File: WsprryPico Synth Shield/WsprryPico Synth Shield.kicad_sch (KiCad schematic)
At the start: 54 parts, among them J11 1x20 socket, J12 1x20 socket, J61 SMA 50ohm, J71 QLG3 GPS Receiver, Q61 BS170, SW81 Push, U31 Si5351A-B-GTR, U41 TPS7A2033, U51 TPS22918, U71 LS7366R-S, U72 SN74LVC1G14, Y21 25MHz TCXO

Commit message: Save Synth layout progress and localize TP71 through-hole footprint
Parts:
- TP71: footprint wsprrypico-synth-shield:TestPoint_Pad_D2.0mm -> wsprrypico-synth-shield:TestPoint_THTPad_1.0x1.0mm_Drill0.5mm
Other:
- moved on the sheet: R73
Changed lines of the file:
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@@
 	)
 	(junction
+		(at 142.24 177.8)
+		(diameter 0)
+		(color 0 0 0 0)
+	)
+	(junction
 		(at 125.73 27.94)
 		(diameter 0)
@@
 		(color 0 0 0 0)
 	)
+	(junction
+		(at 123.19 182.88)
+		(diameter 0)
+		(color 0 0 0 0)
+	)
 	(no_connect
 		(at 189.23 41.91)
@@
 	(wire
 		(pts
+			(xy 124.46 182.88) (xy 123.19 182.88)
+		)
+		(stroke
+			(width 0)
+			(type default)
+		)
+	)
+	(wire
+		(pts
 			(xy 354.33 93.98) (xy 365.76 93.98)
 		)
@@
 	(wire
 		(pts
+			(xy 123.19 182.88) (xy 123.19 177.8)
+		)
+		(stroke
+			(width 0)
+			(type default)
+		)
+	)
+	(wire
+		(pts
 			(xy 158.75 52.07) (xy 170.18 52.07)
 		)
@@
 	(wire
 		(pts
+			(xy 116.84 177.8) (xy 123.19 177.8)
+		)
+		(stroke
+			(width 0)
+			(type default)
+		)
+	)
+	(wire
+		(pts
 			(xy 86.36 138.43) (xy 78.74 138.43)
 		)
@@
 	(wire
 		(pts
+			(xy 143.51 180.34) (xy 142.24 180.34)
+		)
+		(stroke
+			(width 0)
+			(type default)
+		)
+	)
+	(wire
+		(pts
 			(xy 228.6 104.14) (xy 229.87 104.14)
 		)
@@
 	(wire
 		(pts
+			(xy 142.24 177.8) (xy 135.89 177.8)
+		)
+		(stroke
+			(width 0)
+			(type default)
+		)
+	)
+	(wire
+		(pts
 			(xy 138.43 105.41) (xy 138.43 106.68)
 		)
@@
 	(wire
 		(pts
-			(xy 109.22 182.88) (xy 109.22 184.15)
+			(xy 113.03 182.88) (xy 113.03 184.15)
 		)
 		(stroke
@@
 	(wire
 		(pts
+			(xy 138.43 185.42) (xy 143.51 185.42)
+		)
+		(stroke
+			(width 0)
+			(type default)
+		)
+	)
+	(wire
+		(pts
 			(xy 111.76 104.14) (xy 111.76 96.52)
 		)
@@
 	(wire
 		(pts
+			(xy 123.19 182.88) (xy 121.92 182.88)
+		)
+		(stroke
+			(width 0)
+			(type default)
+		)
+	)
+	(wire
+		(pts
 			(xy 90.17 31.75) (xy 90.17 33.02)
 		)
@@
 	(wire
 		(pts
+			(xy 142.24 180.34) (xy 142.24 177.8)
+		)
+		(stroke
+			(width 0)
+			(type default)
+		)
+	)
+	(wire
+		(pts
 			(xy 279.4 41.91) (xy 284.48 41.91)
 		)
@@
 	(wire
 		(pts
-			(xy 110.49 182.88) (xy 109.22 182.88)
+			(xy 114.3 182.88) (xy 113.03 182.88)
 		)
 		(stroke
@@
 	(wire
 		(pts
-			(xy 118.11 182.88) (xy 124.46 182.88)
-		)
-		(stroke
-			(width 0)
-			(type default)
-		)
-	)
-	(wire
-		(pts
 			(xy 111.76 96.52) (xy 110.49 96.52)
 		)
@@
 	(wire
 		(pts
-			(xy 143.51 177.8) (xy 135.89 177.8)
+			(xy 143.51 177.8) (xy 142.24 177.8)
 		)
 		(stroke
@@
 	)
 	(label "GPS_PPS"
-		(at 118.11 182.88 0)
+		(at 116.84 177.8 0)
 		(effects
 			(font
@@
 	)
 	(label "GPS_TX"
-		(at 143.51 185.42 180)
+		(at 138.43 185.42 0)
 		(effects
 			(font
 				(size 1 1)
 			)
-			(justify right bottom)
+			(justify left bottom)
 		)
 	)
@@
 	)
 	(label "GND"
-		(at 110.49 182.88 180)
+		(at 114.3 182.88 180)
 		(effects
 			(font
@@
 		)
 	)
-	(label "PICO_3V3"
-		(at 143.51 180.34 180)
-		(effects
-			(font
-				(size 1 1)
-			)
-			(justify right bottom)
-		)
-	)
 	(label "GND"
 		(at 123.19 55.88 180)
@@
 	(symbol
 		(lib_id "wsprrypico-synth-shield:R")
-		(at 114.3 182.88 180)
+		(at 118.11 182.88 180)
 		(unit 1)
 		(body_style 1)
@@
 		(dnp no)
 		(property "Reference" "R73"
-			(at 116.078 185.166 0)
+			(at 119.888 185.166 0)
 			(show_name no)
 			(do_not_autoplace no)
@@
 		)
 		(property "Value" "100kΩ"
-			(at 117.094 180.34 0)
+			(at 120.904 180.34 0)
 			(show_name no)
 			(do_not_autoplace no)
@@
 		)
 		(property "Footprint" "wsprrypico-synth-shield:R_0603_1608Metric"
-			(at 114.3 182.88 0)
+			(at 118.11 182.88 0)
 			(hide yes)
 			(show_name no)
@@
 		)
 		(property "Datasheet" "https://www.lcsc.com/product-detail/C25803.html"
-			(at 114.3 182.88 0)
+			(at 118.11 182.88 0)
 			(hide yes)
 			(show_name no)
@@
 		)
 		(property "Description" "PPS input default pull-down; 100 kohm; Thick film"
-			(at 114.3 182.88 0)
+			(at 118.11 182.88 0)
 			(hide yes)
 			(show_name no)
@@
 		)
 		(property "Manufacturer" "UNI-ROYAL"
-			(at 114.3 182.88 0)
+			(at 118.11 182.88 0)
 			(hide yes)
 			(show_name no)
@@
 		)
 		(property "MPN" "0603WAF1003T5E"
-			(at 114.3 182.88 0)
+			(at 118.11 182.88 0)
 			(hide yes)
 			(show_name no)
@@
 		)
 		(property "LCSC Part #" "C25803"
-			(at 114.3 182.88 0)
+			(at 118.11 182.88 0)
 			(hide yes)
 			(show_name no)
@@
 		)
 		(property "Supplier URL" "https://www.lcsc.com/product-detail/C25803.html"
-			(at 114.3 182.88 0)
+			(at 118.11 182.88 0)
 			(hide yes)
 			(show_name no)
@@
 		)
 		(property "Specified Value" "100 kohm"
-			(at 114.3 182.88 0)
+			(at 118.11 182.88 0)
 			(hide yes)
 			(show_name no)
@@
 		)
 		(property "Technology" "Thick film"
-			(at 114.3 182.88 0)
+			(at 118.11 182.88 0)
 			(hide yes)
 			(show_name no)
@@
 		)
 		(property "Tolerance" "1%"
-			(at 114.3 182.88 0)
+			(at 118.11 182.88 0)
 			(hide yes)
 			(show_name no)
@@
 		)
 		(property "Rating" "100 mW; 75 V"
-			(at 114.3 182.88 0)
+			(at 118.11 182.88 0)
 			(hide yes)
 			(show_name no)
@@
 		)
 		(property "Assembly" "SMT"
-			(at 114.3 182.88 0)
+			(at 118.11 182.88 0)
 			(hide yes)
 			(show_name no)
@@
 		)
 		(property "Function" "PPS input default pull-down"
-			(at 114.3 182.88 0)
+			(at 118.11 182.88 0)
 			(hide yes)
 			(show_name no)
@@
 		)
 		(property "Selection status" "Selected prototype"
-			(at 114.3 182.88 0)
+			(at 118.11 182.88 0)
 			(hide yes)
 			(show_name no)
@@
 			)
 		)
-		(property "Footprint" "wsprrypico-synth-shield:TestPoint_Pad_D2.0mm"
+		(property "Footprint" "wsprrypico-synth-shield:TestPoint_THTPad_1.0x1.0mm_Drill0.5mm"
 			(at 135.89 146.05 0)
 			(hide yes)
@@
 	(symbol
 		(lib_id "power:GND")
-		(at 109.22 184.15 0)
+		(at 113.03 184.15 0)
 		(mirror y)
 		(unit 1)
@@
 		(dnp no)
 		(property "Reference" "#PWR029"
-			(at 109.22 190.5 0)
+			(at 113.03 190.5 0)
 			(hide yes)
 			(show_name no)
@@
 		)
 		(property "Value" "GND"
-			(at 109.22 187.96 0)
+			(at 113.03 187.96 0)
 			(show_name no)
 			(do_not_autoplace no)
@@
 		)
 		(property "Footprint" ""
-			(at 109.22 184.15 0)
+			(at 113.03 184.15 0)
 			(hide yes)
 			(show_name no)
@@
 		)
 		(property "Datasheet" ""
-			(at 109.22 184.15 0)
+			(at 113.03 184.15 0)
 			(hide yes)
 			(show_name no)
@@
 		)
 		(property "Description" "Power symbol creates a global label with name \"GND\" , ground"
-			(at 109.22 184.15 0)
+			(at 113.03 184.15 0)
 			(hide yes)
 			(show_name no)

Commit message: Add onboard 90-series GPS receiver to Pico synth shield
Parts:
- removed J71: QLG3 GPS Receiver, wsprrypico-synth-shield:QLG3_GPS_UndersideHeader_SinglePost, symbol wsprrypico-synth-shield:Conn_01x05
- added C92, C93: 100nF, wsprrypico-synth-shield:C_0603_1608Metric, symbol wsprrypico-synth-shield:C
- added J91: SMA 50ohm, wsprrypico-synth-shield:SMA_Adafruit_1865_EdgeMount, symbol wsprrypico-synth-shield:SMA
- added L91: 47nH, wsprrypico-synth-shield:L_0603_1608Metric, symbol wsprrypico-synth-shield:L
- added R91: 1kΩ, wsprrypico-synth-shield:R_0603_1608Metric, symbol wsprrypico-synth-shield:R
- added U91: ATGM336H-5N31, wsprrypico-synth-shield:Zhongke_ATGM336H-5N31_9.7x10.1mm_P1.1mm, symbol wsprrypico-synth-shield:ATGM336H_5N31
- C91: renamed from C74; value 2.2μF -> 10uF; footprint wsprrypico-synth-shield:C_0805_2012Metric -> wsprrypico-synth-shield:C_1206_3216Metric; Function GPS header local supply bypass -> GNSS supply bulk; LCSC Part # C364318 -> C77093; MPN CL21B225KAFNFNE -> GRM31CR71E106KA12L; Manufacturer Samsung Electro-Mechanics -> muRata; Specified Value 2.2 uF -> 10 uF; Supplier URL https://www.lcsc.com/product-detail/C364318.html -> https://www.lcsc.com/product-detail/C77093.html
- JP41: footprint wsprrypico-synth-shield:PowerSelector_VBUS_IN_VSYS_Cuttable -> Jumper:SolderJumper-3_P1.3mm_Bridged12_RoundedPad1.0x1.5mm_NumberLabels
- renumbered TP71 to TP91
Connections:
- net GND: now also C92.2, C93.2, J91.2 (GND), U91.1 (GND), U91.10 (GND), U91.12 (GND)
- net GPS_PPS_RAW: now also U91.4 (1PPS)
- net GPS_RX: now also R91.2
- net GPS_TX: now also U91.2 (TXD)
- net PICO_3V3: now also C92.1, C93.1, U91.6 (VBAT), U91.8 (VCC)
- new net GPS_ANT: J91.1 (In), L91.2, U91.11 (RF_IN)
- new net GPS_ANT_BIAS: L91.1, U91.14 (VCC_RF)
- new net GPS_RX_MODULE: R91.1, U91.3 (RXD)
- no-connect marks 20 -> 28
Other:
- note added: "3.3 V UART/PPS. VBAT tied to PICO_3V3; no battery. Active antenna: 47 nH bias feed; 50-ohm RF route. CASIC commands, not GK9501."
- note added: "PPS from 90-series GPS receiver. Counter and PPS conditioner retain 70-series references."
- note removed: "QLG3 underside male pins -> shield TOP female socket. 1=3V3 2=VBAT(3V3) 3=PPS 4=GPS_TX 5=GND"
- moved on the sheet: C91, TP91

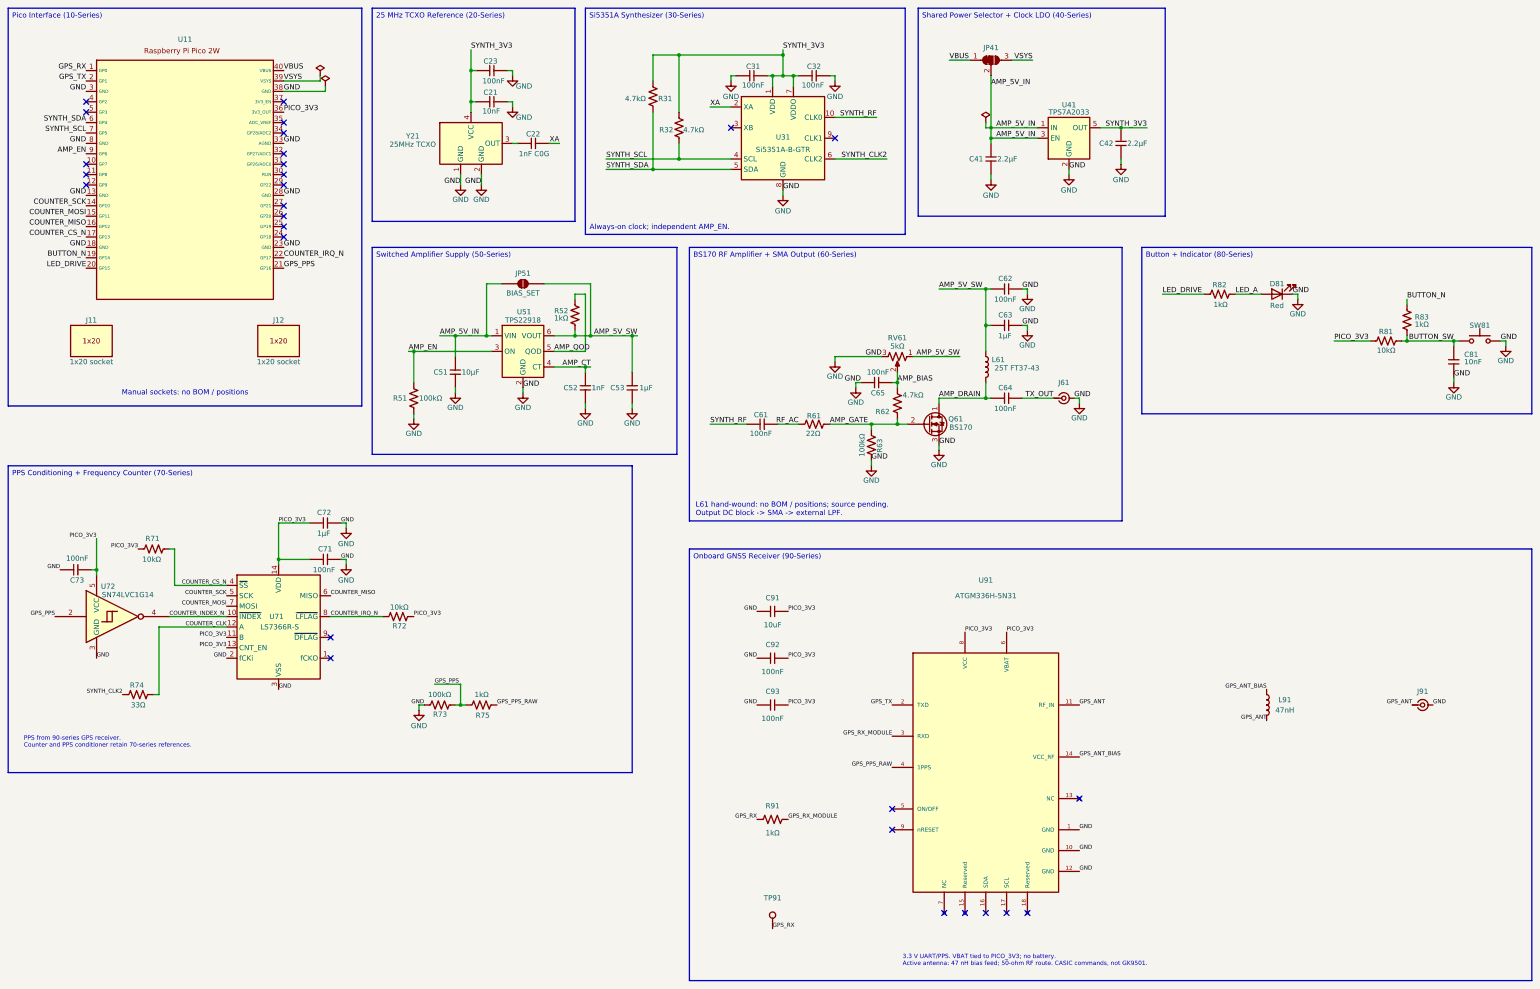
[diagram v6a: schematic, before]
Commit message: Checked through the JLCPCB upload
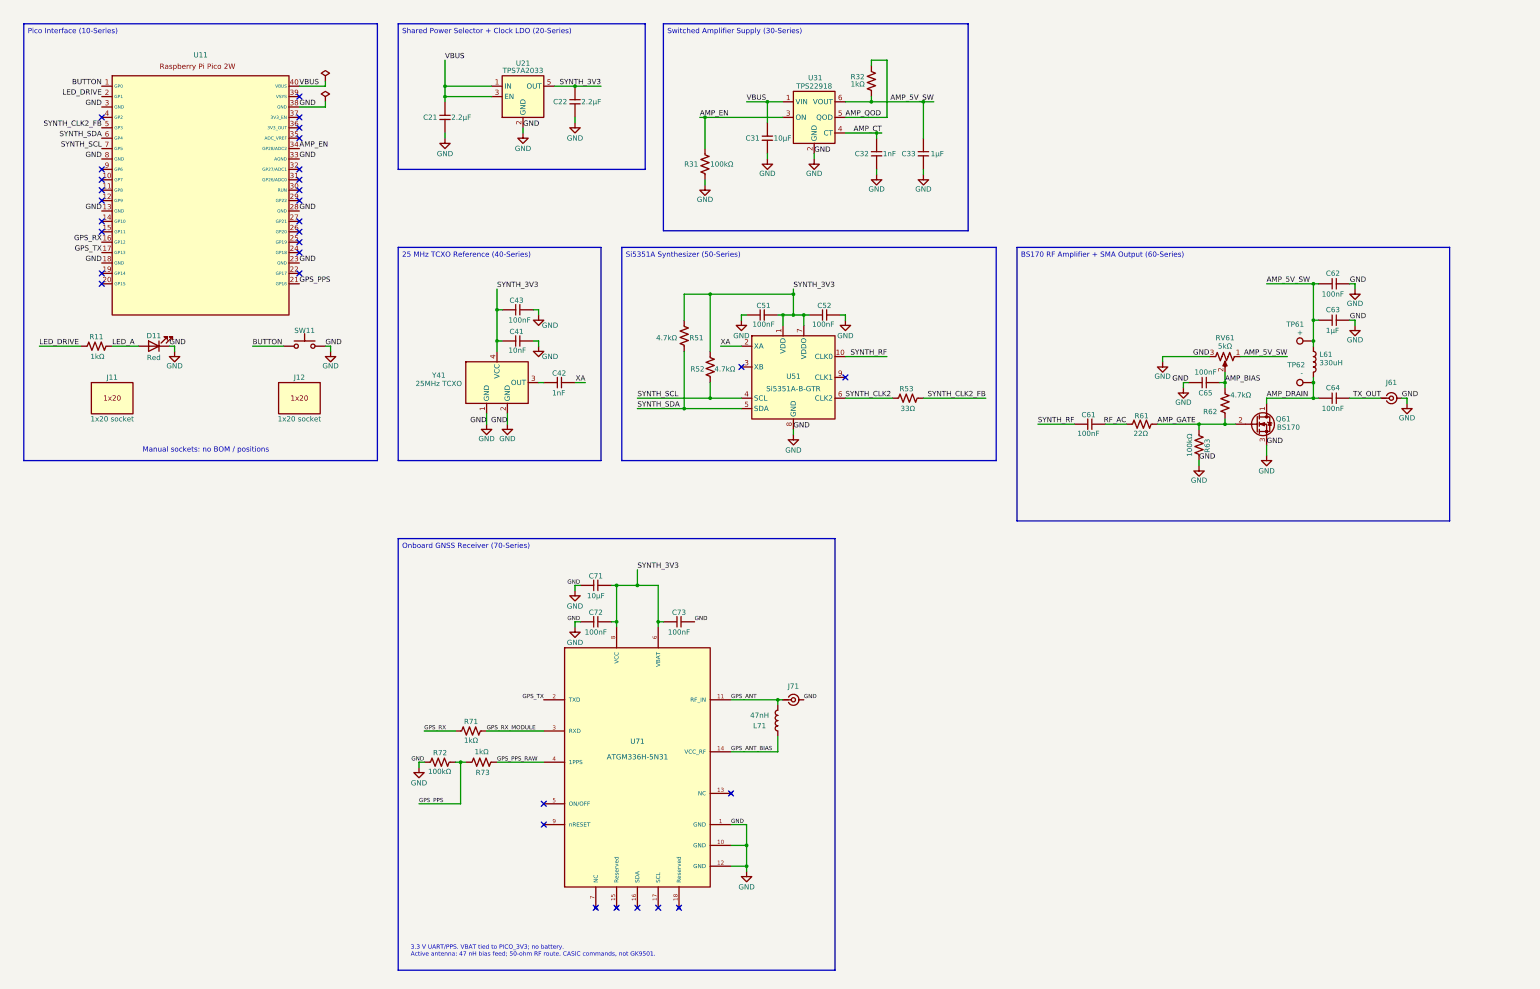
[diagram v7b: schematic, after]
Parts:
- removed C71, C73: 100nF, wsprrypico-synth-shield:C_0603_1608Metric, symbol wsprrypico-synth-shield:C
- removed C72: 1μF, wsprrypico-synth-shield:C_0805_2012Metric, symbol wsprrypico-synth-shield:C
- removed C81: 10nF, wsprrypico-synth-shield:C_0603_1608Metric, symbol wsprrypico-synth-shield:C
- removed JP41: SolderJumper_3_Bridged12, Jumper:SolderJumper-3_P1.3mm_Bridged12_RoundedPad1.0x1.5mm_NumberLabels, symbol wsprrypico-synth-shield:SolderJumper_3_Bridged12
- removed JP51: BIAS_SET, wsprrypico-synth-shield:SolderJumper-2_P1.3mm_Open_RoundedPad1.0x1.5mm, symbol wsprrypico-synth-shield:SolderJumper_2_Open
- removed R71, R72, R81: 10kΩ, wsprrypico-synth-shield:R_0603_1608Metric, symbol wsprrypico-synth-shield:R
- removed R83: 1kΩ, wsprrypico-synth-shield:R_0603_1608Metric, symbol wsprrypico-synth-shield:R
- removed TP91: GPS_RX, wsprrypico-synth-shield:TestPoint_THTPad_1.0x1.0mm_Drill0.5mm, symbol wsprrypico-synth-shield:TestPoint
- removed U71: LS7366R-S, wsprrypico-synth-shield:SOIC-14_3.9x8.7mm_P1.27mm, symbol wsprrypico-synth-shield:LS7366R_S
- removed U72: SN74LVC1G14, wsprrypico-synth-shield:SOT-23-5, symbol wsprrypico-synth-shield:SN74LVC1G14DBVR
- added TP61: +, wsprrypico-synth-shield:TestPoint_THTPad_1.0x1.0mm_Drill0.5mm, symbol wsprrypico-synth-shield:TestPoint
- added TP62: -, wsprrypico-synth-shield:TestPoint_THTPad_1.0x1.0mm_Drill0.5mm, symbol wsprrypico-synth-shield:TestPoint
- C21: renamed from C41; Function Clock LDO input/output capacitors -> Shared LDO input capacitor; LCSC Part # C364318 -> C277470; MPN CL21B225KAFNFNE -> CC0805KKX7R8BB225; Manufacturer Samsung Electro-Mechanics -> YAGEO; Supplier URL https://www.lcsc.com/product-detail/C364318.html -> https://www.lcsc.com/product-detail/C277470.html
- C22: renamed from C42; Function Clock LDO input/output capacitors -> Shared LDO output capacitor; LCSC Part # C364318 -> C277470; MPN CL21B225KAFNFNE -> CC0805KKX7R8BB225; Manufacturer Samsung Electro-Mechanics -> YAGEO; Supplier URL https://www.lcsc.com/product-detail/C364318.html -> https://www.lcsc.com/product-detail/C277470.html
- C31: renamed from C51; LCSC Part # C77093 -> C14860; MPN GRM31CR71E106KA12L -> CL31B106KAHNNNE; Manufacturer Murata -> Samsung Electro-Mechanics; Supplier URL https://www.lcsc.com/product-detail/C77093.html -> https://www.lcsc.com/product-detail/C14860.html
- C32: renamed from C52; LCSC Part # C77026 -> C106246; MPN GRM1885C1H102JA01D -> CC0603JRNPO9BN102; Manufacturer Murata -> YAGEO; Supplier URL https://www.lcsc.com/product-detail/C77026.html -> https://www.lcsc.com/product-detail/C106246.html
- C41: renamed from C21; LCSC Part # C1589 -> C525264; MPN CL10B103KB8NNNC -> FN18X103K500PSG; Manufacturer Samsung Electro-Mechanics -> PSA; Supplier URL https://www.lcsc.com/product-detail/C1589.html -> https://www.lcsc.com/product-detail/C525264.html
- C42: renamed from C22; value 1nF C0G -> 1nF; LCSC Part # C77026 -> C106246; MPN GRM1885C1H102JA01D -> CC0603JRNPO9BN102; Manufacturer Murata -> YAGEO; Supplier URL https://www.lcsc.com/product-detail/C77026.html -> https://www.lcsc.com/product-detail/C106246.html
- C43: renamed from C23; Function TCXO additional bypass; Si5351 VDD/VDDO bypass -> TCXO supply bypass; LCSC Part # C14663 -> C235731; MPN CC0603KRX7R9BB104 -> FN18X104K500PBG; Manufacturer YAGEO -> PSA; Supplier URL https://www.lcsc.com/product-detail/C14663.html -> https://www.lcsc.com/product-detail/C235731.html
- C51: renamed from C31; Function TCXO additional bypass; Si5351 VDD/VDDO bypass -> Si5351A VDD bypass; LCSC Part # C14663 -> C235731; MPN CC0603KRX7R9BB104 -> FN18X104K500PBG; Manufacturer YAGEO -> PSA; Supplier URL https://www.lcsc.com/product-detail/C14663.html -> https://www.lcsc.com/product-detail/C235731.html
- C52: renamed from C32; Function TCXO additional bypass; Si5351 VDD/VDDO bypass -> Si5351A VDDO bypass; LCSC Part # C14663 -> C235731; MPN CC0603KRX7R9BB104 -> FN18X104K500PBG; Manufacturer YAGEO -> PSA; Supplier URL https://www.lcsc.com/product-detail/C14663.html -> https://www.lcsc.com/product-detail/C235731.html
- C61: Function RF input coupling; drain to SMA DC blocking -> RF input DC blocking
- C62, C65: LCSC Part # C14663 -> C235731; MPN CC0603KRX7R9BB104 -> FN18X104K500PBG; Manufacturer YAGEO -> PSA; Supplier URL https://www.lcsc.com/product-detail/C14663.html -> https://www.lcsc.com/product-detail/C235731.html
- C64: Function RF input coupling; drain to SMA DC blocking -> RF output DC blocking
- C71: renamed from C91; value 10uF -> 10μF; Function GNSS supply bulk -> GNSS VCC bulk bypass; LCSC Part # C77093 -> C14860; MPN GRM31CR71E106KA12L -> CL31B106KAHNNNE; Manufacturer muRata -> Samsung Electro-Mechanics; Supplier URL https://www.lcsc.com/product-detail/C77093.html -> https://www.lcsc.com/product-detail/C14860.html
- C72: renamed from C92; Function GNSS VCC local bypass -> GNSS VCC bypass; LCSC Part # C14663 -> C235731; MPN CC0603KRX7R9BB104 -> FN18X104K500PBG; Manufacturer YAGEO -> PSA; Supplier URL https://www.lcsc.com/product-detail/C14663.html -> https://www.lcsc.com/product-detail/C235731.html
- C73: renamed from C93; Function GNSS VBKP local bypass -> GNSS VBAT bypass; LCSC Part # C14663 -> C235731; MPN CC0603KRX7R9BB104 -> FN18X104K500PBG; Manufacturer YAGEO -> PSA; Supplier URL https://www.lcsc.com/product-detail/C14663.html -> https://www.lcsc.com/product-detail/C235731.html
- J71: renamed from J91; value SMA 50ohm -> U.FL 50ohm; footprint wsprrypico-synth-shield:SMA_Adafruit_1865_EdgeMount -> wsprrypico-synth-shield:U.FL_Hirose_U.FL-R-SMT-1_Vertical; symbol wsprrypico-synth-shield:SMA -> wsprrypico-synth-shield:U_FL; Function GNSS active antenna SMA input -> GNSS active antenna U.FL input; LCSC Part # (none) -> C88373; MPN 1865 -> U.FL-R-SMT-1(10); Manufacturer Adafruit -> Hirose; Selection status Existing project edge-mount footprint selected; manual fit -> Selected U.FL/MHF1 mate; LCSC and JLCPCB availability check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; Specified Value 50 ohm SMA female; board-edge mount; 1.6 mm PCB -> 50 ohm U.FL SMT board receptacle; male center contact; Supplier URL https://www.adafruit.com/product/1865 -> https://www.lcsc.com/product-detail/C88373.html; Technology Edge-launch coaxial connector -> SMT snap-on micro coaxial connector
- L61: value 25T FT37-43 -> 330uH; footprint wsprrypico-synth-shield:L_Toroid_FT37-43_Vertical_P5.08mm -> wsprrypico-synth-shield:L_TDK_VLS6045EX_VLS6045AF; symbol wsprrypico-synth-shield:L -> wsprrypico-synth-shield:VLS6045EX_331M; Assembly Manual -> SMT; LCSC Part # (none) -> C501933; MPN FT37-43 core + hand winding -> VLS6045EX-331M; Manufacturer Amidon / Fair-Rite equivalent to verify -> TDK; Rating DC-bias and RF acceptance required -> 500 mA at 30% L reduction; 470 mA at 40 C rise; DCR 1.872 o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; Selection status Sourcing conflict; awaiting user choice -> Selected prototype 2026-10-10; RF/DC-bias qualification pen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; Specified Value 25 turns on FT37-43; nominal about219uH -> 330 uH at 100 kHz; Supplier URL (none) -> https://www.lcsc.com/product-detail/C501933.html; Technology Ferrite; 43 material -> Factory wirewound ferrite; magnetic shield; SMT; Tolerance Winding/lot dependent -> 20%; now in the parts list
- R11: renamed from R82; LCSC Part # C2907002 -> C22548; MPN FRC0603F1001TS -> RC0603FR-071KL; Manufacturer FOJAN -> YAGEO; Supplier URL https://www.lcsc.com/product-detail/C2907002.html -> https://www.lcsc.com/product-detail/C22548.html
- R32: renamed from R52; LCSC Part # C2907002 -> C22548; MPN FRC0603F1001TS -> RC0603FR-071KL; Manufacturer FOJAN -> YAGEO; Supplier URL https://www.lcsc.com/product-detail/C2907002.html -> https://www.lcsc.com/product-detail/C22548.html
- R51: renamed from R31; LCSC Part # C23162 -> C99782; MPN 0603WAF4701T5E -> RC0603FR-074K7L; Manufacturer UNI-ROYAL -> YAGEO; Supplier URL https://www.lcsc.com/product-detail/C23162.html -> https://www.lcsc.com/product-detail/C99782.html
- R52: renamed from R32; LCSC Part # C23162 -> C99782; MPN 0603WAF4701T5E -> RC0603FR-074K7L; Manufacturer UNI-ROYAL -> YAGEO; Supplier URL https://www.lcsc.com/product-detail/C23162.html -> https://www.lcsc.com/product-detail/C99782.html
- R62: LCSC Part # C23162 -> C99782; MPN 0603WAF4701T5E -> RC0603FR-074K7L; Manufacturer UNI-ROYAL -> YAGEO; Supplier URL https://www.lcsc.com/product-detail/C23162.html -> https://www.lcsc.com/product-detail/C99782.html
- R71: renamed from R91; Function GPS command UART series damping -> Pico to GNSS UART series resistor; LCSC Part # C2907002 -> C22548; MPN FRC0603F1001TS -> RC0603FR-071KL; Manufacturer FOJAN -> YAGEO; Supplier URL https://www.lcsc.com/product-detail/C2907002.html -> https://www.lcsc.com/product-detail/C22548.html
- R73: renamed from R75; LCSC Part # C2907002 -> C22548; MPN FRC0603F1001TS -> RC0603FR-071KL; Manufacturer FOJAN -> YAGEO; Supplier URL https://www.lcsc.com/product-detail/C2907002.html -> https://www.lcsc.com/product-detail/C22548.html
- RV61: Manufacturer Bourns -> BOURNS
- U71: renamed from U91; FT Rotation Offset (none) -> 90
- renumbered C53 to C33, D81 to D11, L91 to L71, R51 to R31, R74 to R53, R73 to R72, SW81 to SW11, U41 to U21, U51 to U31, U31 to U51, Y21 to Y41
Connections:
- net AMP_5V_IN is gone; now on net VBUS: C21.1, C31.1, U21.1 (IN), U21.3 (EN), U31.1 (VIN)
- net COUNTER_CLK is gone; now on net SYNTH_CLK2_FB: R53.2
- net COUNTER_CS_N is gone; now on net GPS_TX: U11.17 (GP13)
- net COUNTER_MISO is gone; now on net GPS_RX: U11.16 (GP12)
- net AMP_5V_SW: now also TP61.1
- net AMP_DRAIN: now also TP62.1
- net AMP_EN: now also U11.34 (GP28/ADC2); no longer U11.9 (GP6)
- net GPS_RX: no longer U11.1 (GP0)
- net GPS_TX: no longer U11.2 (GP1)
- net LED_DRIVE: now also U11.2 (GP1); no longer U11.20 (GP15)
- net SYNTH_3V3: now also C71.1, C72.1, C73.1, U71.6 (VBAT), U71.8 (VCC)
- net SYNTH_CLK2_FB: now reaches U11.5 (GP3)
- net BUTTON_N: no longer names the net of U11.19 (GP14)
- net BUTTON_SW renamed BUTTON
- net BUTTON: now also U11.1 (GP0)
- net COUNTER_IRQ_N: no longer names the net of U11.22 (GP17)
- net COUNTER_MOSI: no longer names the net of U11.15 (GP11)
- net COUNTER_SCK: no longer names the net of U11.14 (GP10)
- removed net PICO_3V3: C71.1, C72.1, C73.1, U11.36 (3V3_OUT), U71.6 (VBAT), U71.8 (VCC)
- net VSYS: no longer names the net of U11.39 (VSYS)
- no-connect marks 28 -> 32
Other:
- note removed: "Always-on clock; independent AMP_EN."
- note removed: "L61 hand-wound: no BOM / positions; source pending. Output DC block -> SMA -> external LPF."
- note removed: "PPS from 90-series GPS receiver. Counter and PPS conditioner retain 70-series references."
- moved on the sheet: C21, C22, C31, C32, C33, C41, C42, C43, C51, C52, C61, C62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
